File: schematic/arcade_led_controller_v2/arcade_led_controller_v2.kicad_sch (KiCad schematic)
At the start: 58 parts, among them P1_BALLTOP_LED_1 WS2812B, P1_BUTTONS_LED1 WS2812B, P1_DP_JOY_MODE_LED1 LED, P1_JOYSTICK_LED1 WS2812B, P1_LS_JOY_MODE_LED1 LED, P1_RS_JOY_MODE_LED1 LED, P2_BALLTOP_LED_1 WS2812B, P2_BUTTONS_LED1 WS2812B, P2_DP_JOY_MODE_LED1 LED, P2_JOYSTICK_LED1 WS2812B, P2_LS_JOY_MODE_LED1 LED, P2_RS_JOY_MODE_LED1 LED, Q1 Q_NMOS_GDS, Q2 Q_NMOS_GDS, Q3 Q_NMOS_GDS, Q4(PN2222)1 PN2222A, Q5(PN222)1 PN2222A, Q6(PN2222)1 PN2222A, Q7(PN2222)1 PN2222A, U1 74AHCT125, U2 74AHCT125, U3 EA_DOGL128X-6

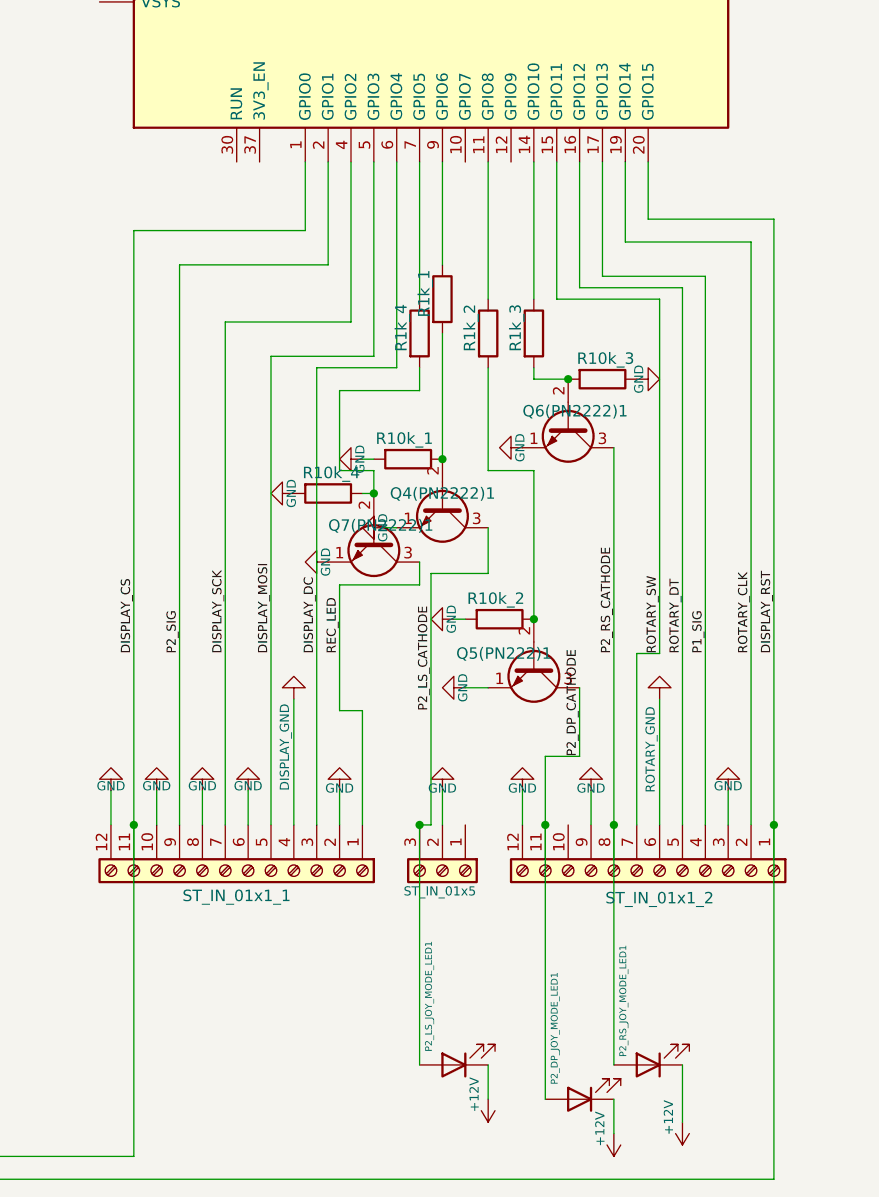
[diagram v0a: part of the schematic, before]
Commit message: Update input pin assignments
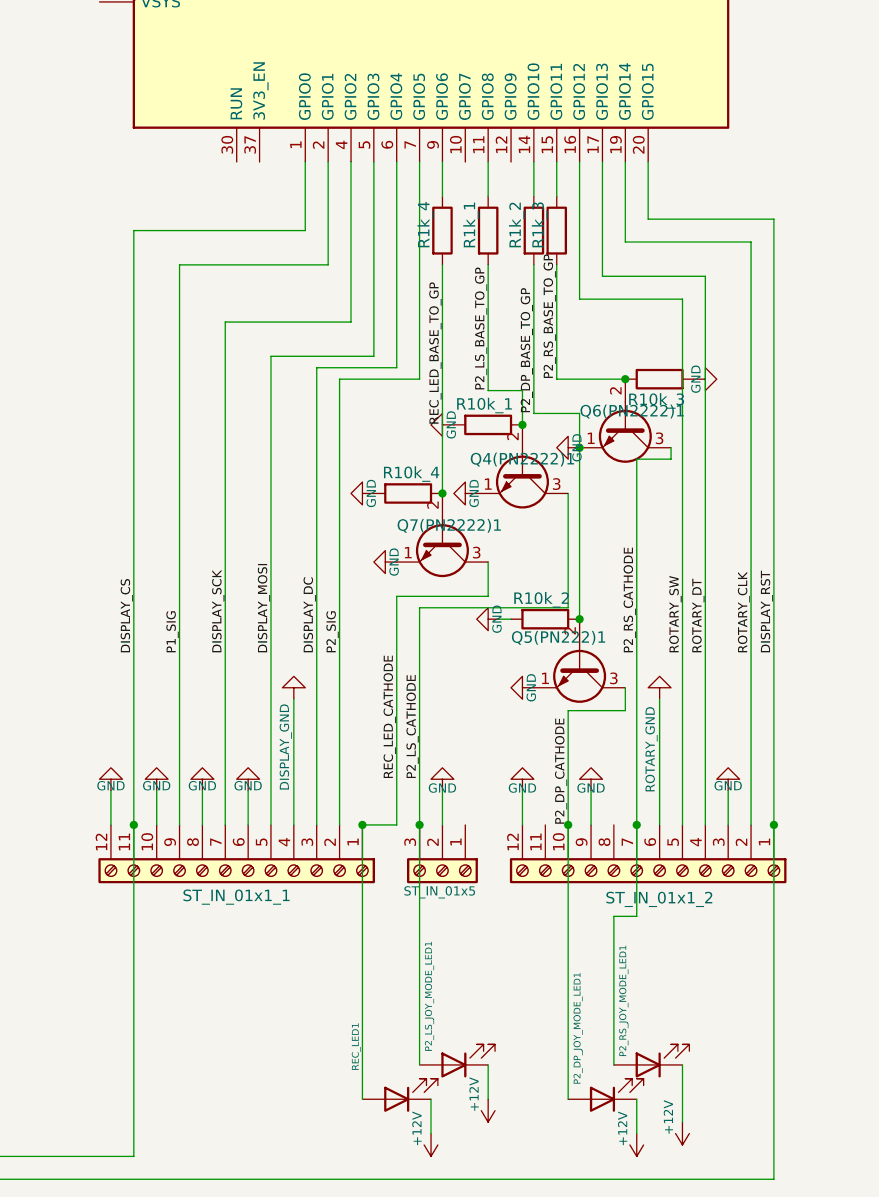
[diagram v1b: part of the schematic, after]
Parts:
- added REC_LED1: LED, LED_THT:LED_D1.8mm_W1.8mm_H2.4mm_Horizontal_O3.81mm_Z1.6mm, symbol Device:LED
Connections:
- net +12V: now also REC_LED1.1 (K)
- net GND: now also Q5(PN222)1.2 (B), R10k_2.1, R10k_3.2, R1k_2.2; no longer R10k_3.1, ST_IN_01x1_1.2 (Pin_2)
- net P1_SIG: now also A1.2 (GPIO1), ST_IN_01x1_1.9 (Pin_9); no longer A1.17 (GPIO13), ST_IN_01x1_2.4 (Pin_4)
- net P2_DP_CATHODE: now also ST_IN_01x1_2.10 (Pin_10); no longer ST_IN_01x1_2.11 (Pin_11)
- net P2_RS_CATHODE: now also ST_IN_01x1_2.7 (Pin_7); no longer ST_IN_01x1_2.8 (Pin_8)
- net P2_SIG: now also A1.7 (GPIO5), ST_IN_01x1_1.2 (Pin_2); no longer A1.2 (GPIO1), ST_IN_01x1_1.9 (Pin_9)
- net ROTARY_DT: now also A1.17 (GPIO13), ST_IN_01x1_2.4 (Pin_4); no longer A1.16 (GPIO12), ST_IN_01x1_2.5 (Pin_5)
- net ROTARY_SW: now also A1.16 (GPIO12), ST_IN_01x1_2.5 (Pin_5); no longer A1.15 (GPIO11), ST_IN_01x1_2.7 (Pin_7)
- net P2_RS_BASE_TO_GP: now reaches Q6(PN2222)1.2 (B), R1k_3.2
- net P2_RS_BASE_TO_GP: now also R10k_3.1; no longer R10k_3.2
- net REC_LED_BASE_TO_GP: now reaches Q7(PN2222)1.2 (B), R10k_4.1, R1k_4.2
- net at R1k_4.1: now also A1.9 (GPIO6); no longer A1.7 (GPIO5)
- net at R1k_2.1: now also A1.14 (GPIO10); no longer A1.11 (GPIO8)
- net at R1k_3.1: now also A1.15 (GPIO11); no longer A1.14 (GPIO10)
- net at R1k_1.1: now also A1.11 (GPIO8); no longer A1.9 (GPIO6)
- net P2_LS_BASE_TO_GP: now reaches Q4(PN2222)1.2 (B), R10k_1.1, R1k_1.2
- net REC_LED renamed REC_LED_CATHODE
- net REC_LED_CATHODE: now also REC_LED1.2 (A)
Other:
- moved on the sheet: P2_DP_JOY_MODE_LED1, Q4(PN2222)1, Q5(PN222)1, Q6(PN2222)1, Q7(PN2222)1, R10k_1, R10k_2, R10k_3, R10k_4, R1k_1, R1k_2, R1k_3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

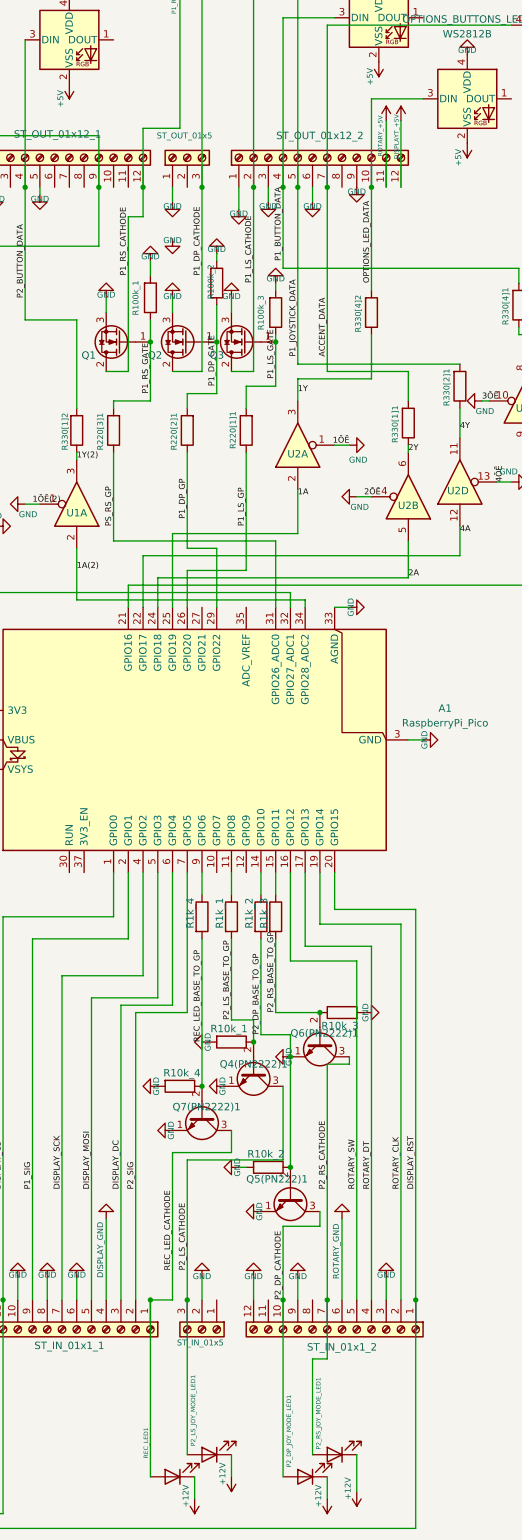
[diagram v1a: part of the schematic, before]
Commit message: complete track routing
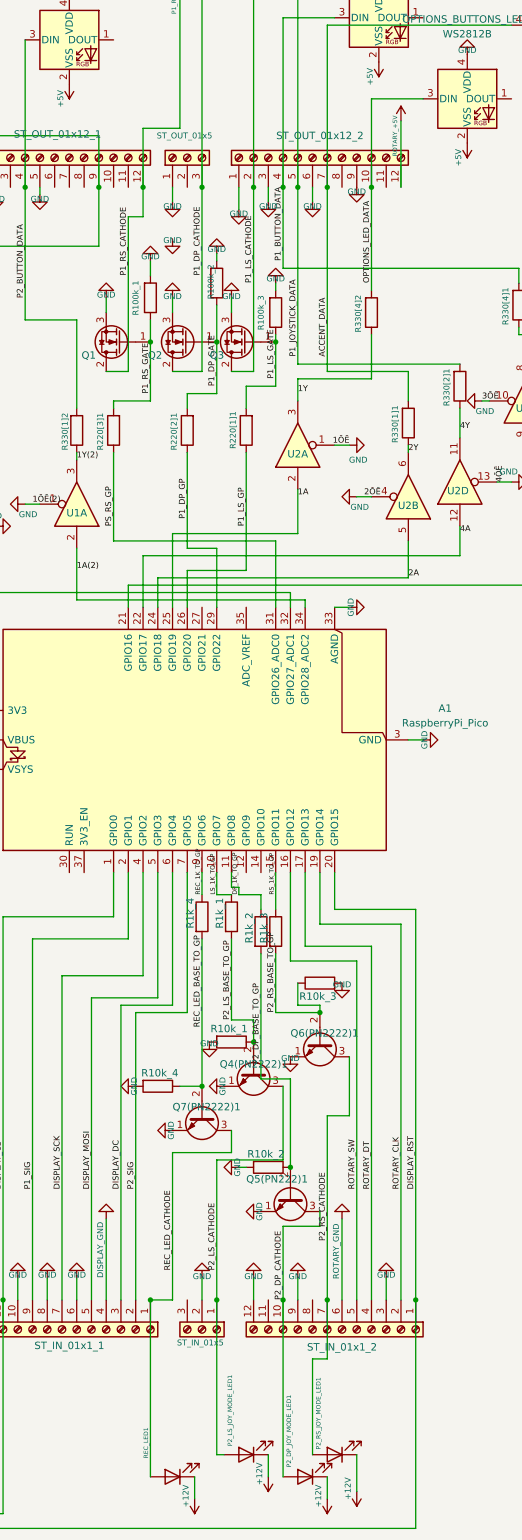
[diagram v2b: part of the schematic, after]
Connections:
- net DISPLAYT_+5V is gone; now on net ROTARY_+5V: ST_OUT_01x12_2.12 (Pin_12)
- net GND: no longer Q5(PN222)1.2 (B), R10k_2.1, R1k_2.2
- net P2_LS_CATHODE: now also ST_IN_01x5.1 (Pin_1); no longer ST_IN_01x5.3 (Pin_3)
- net ROTARY_+5V: no longer ST_OUT_01x12_2.11 (Pin_11)
- net REC_1K_TO_GP: now reaches A1.9 (GPIO6), R1k_4.1
- net at A1.14 (GPIO10): no longer R1k_2.1
- net LS_1K_TO_GP: now reaches A1.10 (GPIO7)
- net LS_1K_TO_GP: now also R1k_1.1
- net DP_1K_TO_GP: now reaches A1.11 (GPIO8)
- net DP_1K_TO_GP: now also R1k_2.1; no longer R1k_1.1
- net RS_1K_TO_GP: now reaches A1.15 (GPIO11), R1k_3.1
- new net P2_DP_BASE_TO_GP: Q5(PN222)1.2 (B), R10k_2.1, R1k_2.2
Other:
- moved on the sheet: P2_LS_JOY_MODE_LED1, R10k_3, R10k_4, R1k_2, R1k_3

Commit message: wrapping up v2 schematic and pcb changes. Update pins.h to match
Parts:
- removed GND_BUS_1, GND_BUS_2: Conn_01x05_Pin, Connector_Wago:Wago_734-165_1x05_P3.50mm_Horizontal, symbol Connector:Conn_01x05_Pin
- added +12V_BUS_1, +12V_BUS_2: Conn_01x05_Pin, TerminalBlock_WAGO:TerminalBlock_WAGO_233-505_2x05_P2.54mm, symbol Connector:Conn_01x05_Pin
- added J1: GND_BUS_1, TerminalBlock_WAGO:TerminalBlock_WAGO_233-506_2x06_P2.54mm, symbol Connector:Conn_01x06_Pin
- added J2: GND_BUS_2, TerminalBlock_WAGO:TerminalBlock_WAGO_233-504_2x04_P2.54mm, symbol Connector:Conn_01x04_Pin
- added J3: PSU_GND_BUS, Connector_Wago:Wago_734-163_1x03_P3.50mm_Horizontal, symbol Connector:Conn_01x03_Pin
- added SW1: RotaryEncoder_Switch, symbol Device:RotaryEncoder_Switch
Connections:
- net +12V: now also +12V_BUS_1.1 (Pin_1), +12V_BUS_1.2 (Pin_2), +12V_BUS_1.3 (Pin_3), +12V_BUS_1.4 (Pin_4), +12V_BUS_1.5 (Pin_5), +12V_BUS_2.1 (Pin_1), +12V_BUS_2.2 (Pin_2), +12V_BUS_2.3 (Pin_3), +12V_BUS_2.4 (Pin_4), +12V_BUS_2.5 (Pin_5)
- net GND: now also J1.1 (Pin_1), J1.2 (Pin_2), J1.3 (Pin_3), J1.4 (Pin_4), J1.5 (Pin_5), J1.6 (Pin_6), J2.1 (Pin_1), J2.2 (Pin_2), J2.3 (Pin_3), J2.4 (Pin_4), J3.1 (Pin_1), J3.2 (Pin_2), J3.3 (Pin_3)
